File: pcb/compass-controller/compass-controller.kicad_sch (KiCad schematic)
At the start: 75 parts, among them J5 ENCODER BUTTON, J6 LEFT BUTTON, J7 X LIM, J8 X LIM, J9 LEFT BUTTON, SW1 TS1187

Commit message: build platform
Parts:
- added C?: 100n, symbol Device:C_Small
- added J10: PMW_0, symbol Connector_Generic:Conn_01x08
- added J11: PMW_1, symbol Connector_Generic:Conn_01x08
- added J12: PMW_2, symbol Connector_Generic:Conn_01x08
- added J13: PMW_3, symbol Connector_Generic:Conn_01x08
- added J?: TC2030, Connector:Tag-Connect_TC2030-IDC-FP_2x03_P1.27mm_Vertical, symbol Connector:Conn_ARM_SWD_TagConnect_TC2030
- added R57: 220R, symbol Device:R_Small_US
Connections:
- net +3V3: now also J10.1 (Pin_1), J11.1 (Pin_1), J12.1 (Pin_1), J13.1 (Pin_1), J?.1 (VCC)
- net GND: now also J10.3 (Pin_3), J10.5 (Pin_5), J10.7 (Pin_7), J11.3 (Pin_3), J11.5 (Pin_5), J11.7 (Pin_7), J12.3 (Pin_3), J12.5 (Pin_5), J12.7 (Pin_7), J13.3 (Pin_3), J13.5 (Pin_5), J13.7 (Pin_7), J?.5 (GND); no longer J?.A1 (GND), J?.A12 (GND), J?.B1 (GND), J?.B12 (GND)
- net PMW_MISO: now also J10.6 (Pin_6), J11.6 (Pin_6), J12.6 (Pin_6), J13.6 (Pin_6)
- net PMW_MOSI: now also J10.4 (Pin_4), J11.4 (Pin_4), J12.4 (Pin_4), J13.4 (Pin_4)
- net PMW_SCK: now also J10.2 (Pin_2), J11.2 (Pin_2), J12.2 (Pin_2), J13.2 (Pin_2)
- net SWCLK: now also J?.4 (SWCLK)
- net SWDIO: now also J?.2 (SWDIO)
- net ~{nRST}: now also J?.3 (~{RESET})
- net Earth: now reaches J?.S1 (SHIELD)
- net Earth: now also C?.1, R57.1
- new net: C?.2, J?.A1 (GND), J?.A12 (GND), J?.B1 (GND), J?.B12 (GND), R57.2
- new net PMW_CS0: J10.8 (Pin_8)
- new net PMW_CS1: J11.8 (Pin_8)
- new net PMW_CS2: J12.8 (Pin_8)
- new net PMW_CS3: J13.8 (Pin_8)
- no-connect marks 5 -> 6
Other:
- moved on the sheet: J?, R31

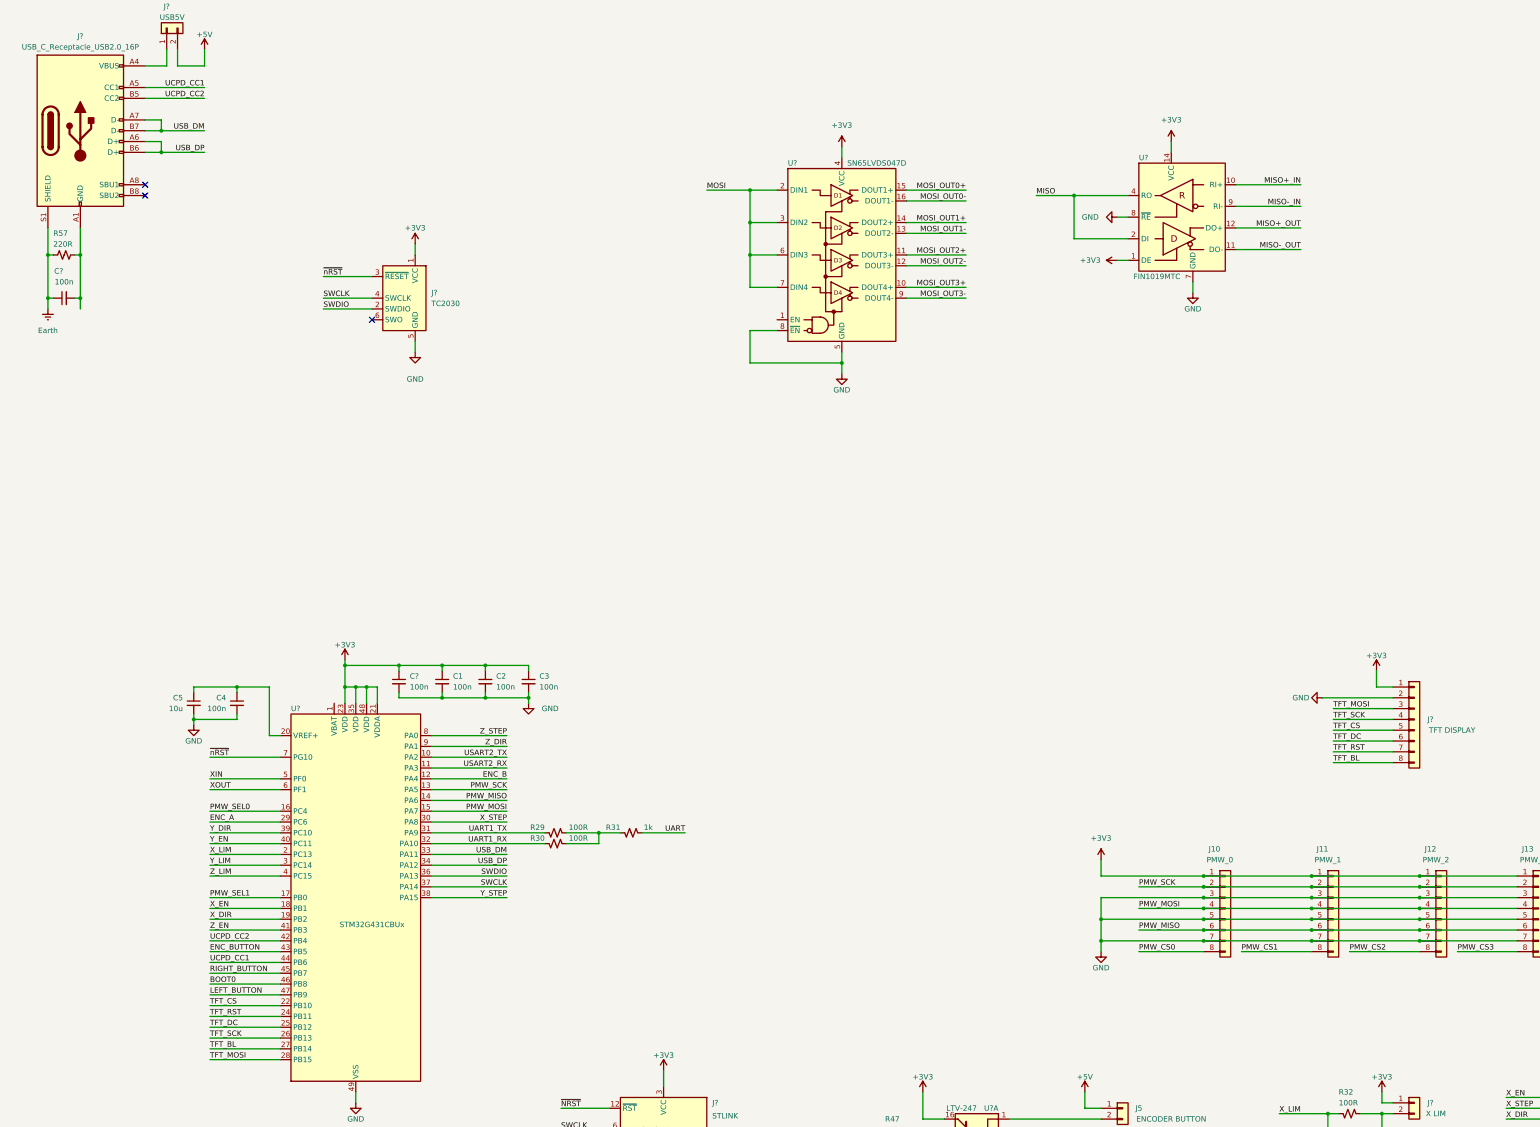
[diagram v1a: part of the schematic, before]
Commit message: update pinout to support SD card
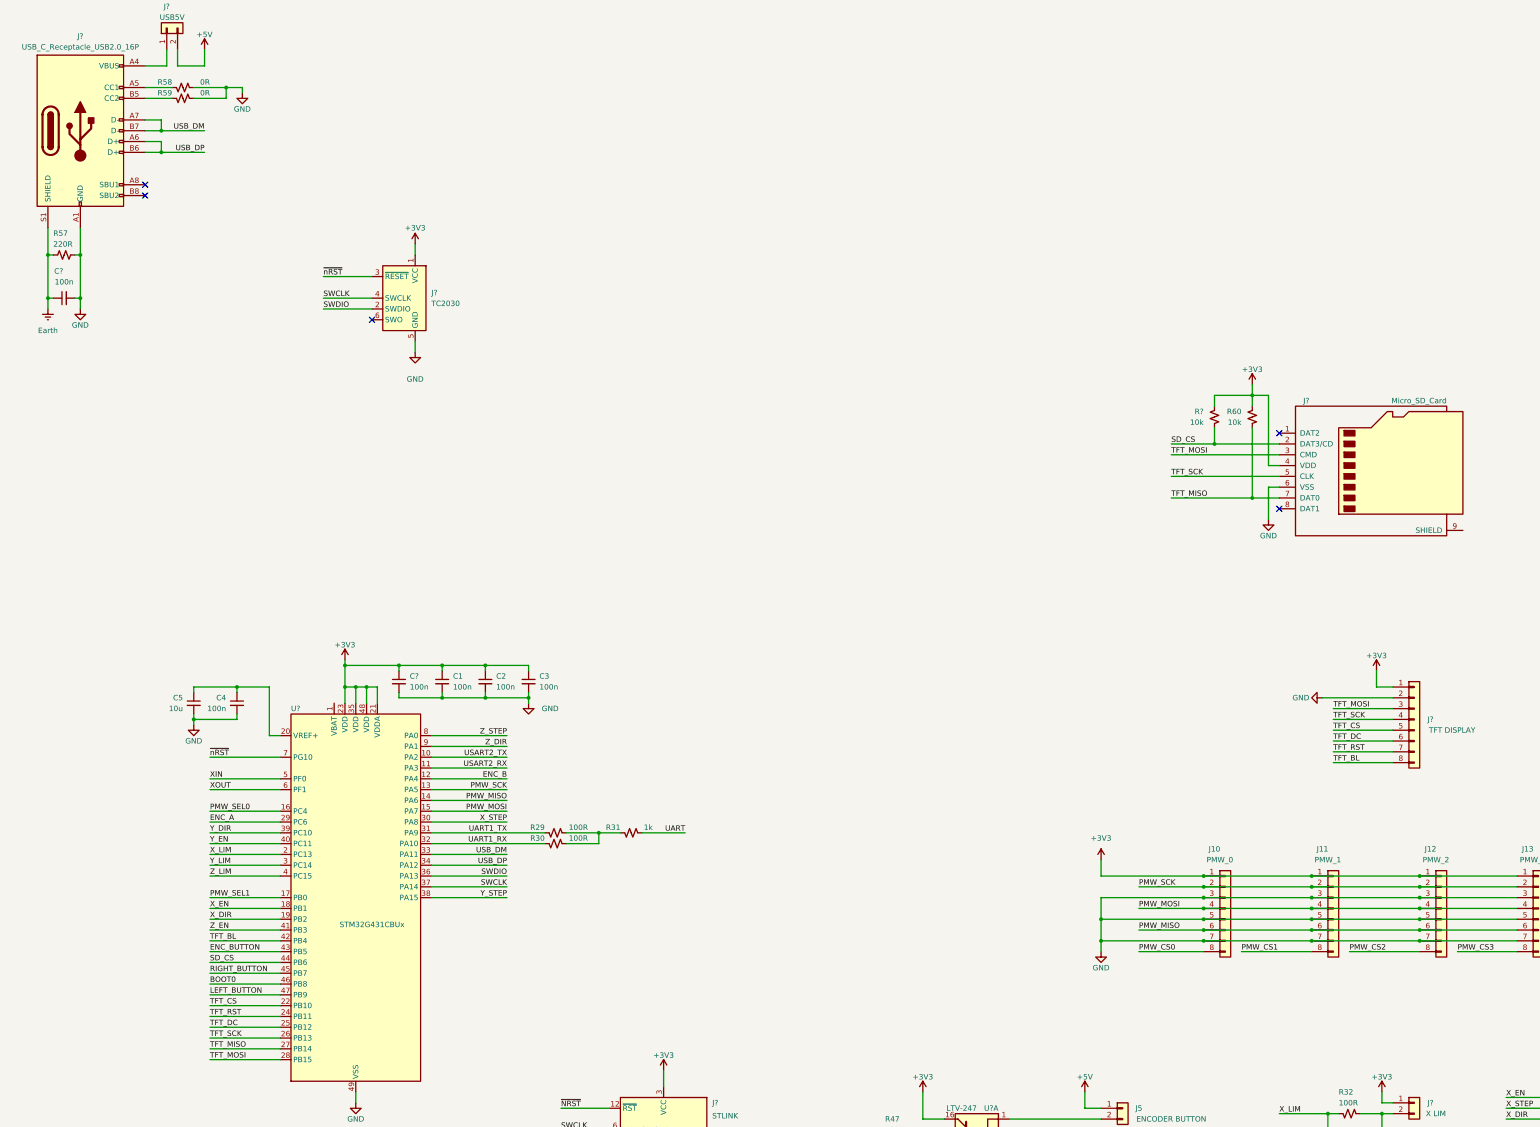
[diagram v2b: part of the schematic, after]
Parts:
- removed U?: FIN1019MTC, Package_SO:TSSOP-14_4.4x5mm_P0.65mm, symbol Interface:FIN1019MTC
- removed U?: SN65LVDS047D, Package_SO:SOIC-16_3.9x9.9mm_P1.27mm, symbol Interface:SN65LVDS047D
- added J?: Micro_SD_Card, symbol Connector:Micro_SD_Card
- added R58, R59: 0R, symbol Device:R_Small_US
- added R60, R?: 10k, symbol Device:R_Small_US
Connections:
- net +3V3: now also J?.4 (VDD), R60.1, R?.1
- net GND: now also C?.2, J?.A1 (GND), J?.A12 (GND), J?.B1 (GND), J?.B12 (GND), R57.2, J?.6 (VSS), R58.2, R59.2
- net TFT_BL: now also U?.42 (PB4); no longer U?.27 (PB14)
- net TFT_MOSI: now also J?.3 (CMD)
- net TFT_SCK: now also J?.5 (CLK)
- net UCPD_CC1: no longer names the net of J?.A5 (CC1)
- net UCPD_CC1: now also R58.1; no longer U?.44 (PB6)
- net UCPD_CC2: no longer names the net of J?.B5 (CC2)
- net UCPD_CC2: now also R59.1; no longer U?.42 (PB4)
- new net SD_CS: J?.2 (DAT3/CD), R?.2, U?.44 (PB6)
- new net TFT_MISO: J?.7 (DAT0), R60.2, U?.27 (PB14)
- no-connect marks 6 -> 8

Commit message: work on schematic
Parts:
- added C301, C305, C306: 10u, Capacitor_SMD:C_1206_3216Metric, symbol Device:C_Small
- added C302: 1u, Capacitor_SMD:C_0603_1608Metric, symbol Device:C_Small
- added C303: 10n, Capacitor_SMD:C_0402_1005Metric, symbol Device:C_Small
- added C304: 100u, Capacitor_SMD:CP_Elec_5x5.4, symbol Device:C_Polarized_Small_US
- added C307: 100n, Capacitor_SMD:C_1206_3216Metric, symbol Device:C_Small
- added D1, D10, D11, D12, D2, D3, D4, D5, D6, D7, D8, D9, D? (x2): WHT, symbol Device:LED
- added D301, D302, D303: SS14, Diode_SMD:D_SMA, symbol Device:D_Schottky
- added J14: Barrel_Jack, symbol Connector:Barrel_Jack
- added L301: 15u, easyeda2kicad:IND-SMD_L8.0-W8.0, symbol Device:L
- added R303: 5k1, Resistor_SMD:R_0603_1608Metric, symbol Device:R_Small_US
- added R304: 100k, Resistor_SMD:R_0603_1608Metric, symbol Device:R_Small_US
- added R305: 10k, Resistor_SMD:R_0603_1608Metric, symbol Device:R_Small_US
- added R306: 3k24, Resistor_SMD:R_0603_1608Metric, symbol Device:R_Small_US
- added R307, R308, R309: 0R, symbol Device:R_Small_US
- added R61: 5k1, symbol Device:R_Small_US
- added R62, R67, R68, R69, R70, R?: 2k2, symbol Device:R_Small_US
- added R63, R64, R65, R66: 10k, symbol Device:R_Small_US
- added R?: 22k, symbol Device:R_Small_US
- added U3, U?: TXU0304PWR, easyeda2kicad:TSSOP-14_L5.0-W4.4-P0.65-LS6.4-BL, symbol easyeda2kicad:TXU0304PWR
- added U301: TPS5430DDA, Package_SO:TI_SO-PowerPAD-8_ThermalVias, symbol Regulator_Switching:TPS5430DDA
- added U?: TPSPX3819M5-L-3-3, easyeda2kicad:SOT-23-5_L3.0-W1.6-P0.95-LS2.8-BR, symbol easyeda2kicad:TPSPX3819M5-L-3-3
- added U?: 74LS138PWR, symbol 74xx:74LS138
- J10, J11, J12, J13: symbol Connector_Generic:Conn_01x08 -> Connector_Generic_Shielded:Conn_01x08_Shielded
- R37, R40, R42, R44, R57: value 220R -> 330R
- R38, R45, R46: value 10k -> 2k2
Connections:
- net +3V3: now also C306.1, C307.1, D2.2 (A), D3.2 (A), D4.2 (A), D5.2 (A), D6.2 (A), D?.2 (A), R308.2, R63.1, R64.1, R65.1, R66.1, U?.16 (VCC)
- net +5V: now also C305.1, D1.2 (A), R307.2, U?.1 (VIN), U?.3 (EN)
- net Earth: now also J10.SH (Shield), J11.SH (Shield), J12.SH (Shield), J13.SH (Shield)
- net GND: now also C301.2, C302.2, C304.2, C305.2, C306.2, C307.2, D301.2 (A), D302.2 (A), J14.2, R303.2, R306.2, R61.2, R62.2, R?.2, U301.6 (GND), U301.9 (GNDPAD), U?.2 (GND), U?.4 (E1), U?.5 (E2), U?.8 (GND)
- net TFT_MISO: no longer J?.7 (DAT0), R60.2
- net TFT_MOSI: no longer J?.3 (CMD), J?.3 (Pin_3)
- net TFT_SCK: no longer J?.4 (Pin_4), J?.5 (CLK)
- net at R43.1, R50.2: now also D10.1 (K); no longer U?.9
- net at R41.1, R49.2: now also D9.1 (K); no longer U?.11
- net at R38.1, R47.2: now also D7.1 (K); no longer U?.15
- net at R45.1, R52.2: now also D12.1 (K); no longer J6.2 (Pin_2)
- net at R46.1, R51.2: now also D11.1 (K); no longer J9.2 (Pin_2)
- net at R39.1, R48.2: now also D8.1 (K); no longer U?.13
- net PMW_CS0 renamed SPI1_CS0
- net SPI1_CS0: now also R?.2, U?.15 (O0)
- net PMW_CS1 renamed SPI1_CS1
- net SPI1_CS1: now also R67.2, U?.14 (O1)
- net PMW_CS2 renamed SPI1_CS2
- net SPI1_CS2: now also R68.2, U?.13 (O2)
- net PMW_CS3 renamed SPI1_CS3
- net SPI1_CS3: now also R69.2, U?.12 (O3)
- net PMW_MISO renamed SPI1_MISO
- net PMW_MOSI renamed SPI1_MOSI
- net SPI1_MOSI: now also J?.3 (Pin_3)
- net PMW_SCK renamed SPI1_SCK
- net SPI1_SCK: now also J?.4 (Pin_4)
- net PMW_SEL0 renamed SPI1_SEL0
- net SPI1_SEL0: now also U?.1 (A0)
- net PMW_SEL1 renamed SPI1_SEL1
- net SPI1_SEL1: now also R64.2, R65.2, U?.2 (A1)
- net TFT_CS renamed SPI1_CS4
- net SPI1_CS4: now also R70.2, U?.11 (O4); no longer U?.22 (PB10)
- new net: D1.1 (K), R61.1
- new net: D2.1 (K), R62.1
- new net: C304.1, D303.2 (A), L301.2, R305.1
- new net: D3.1 (K), R67.1
- new net: D303.1 (K), R307.1
- new net: D?.1 (K), R?.1 (x2)
- new net: D4.1 (K), R68.1
- new net: D9.2 (A), U?.11
- new net: C302.1, R304.2, U301.5 (EN)
- new net: D11.2 (A), J9.2 (Pin_2)
- new net: D6.1 (K), R70.1
- new net: D7.2 (A), U?.15
- new net: D5.1 (K), R69.1
- new net: R308.1, U?.5 (VOUT)
- new net: C303.1, U301.1 (BOOT)
- new net: J14.1, R309.1
- new net: D8.2 (A), U?.13
- new net: D12.2 (A), J6.2 (Pin_2)
- new net: R63.2, U?.6 (E3)
- new net: D10.2 (A), U?.9
- new net +24V: C301.1, D301.1 (K), D?.2 (A), R303.1, R304.1, R309.2, U301.7 (VIN)
- new net FB: R305.2, R306.1, U301.4 (VSENSE)
- new net SPI1_SEL2: R66.2, U?.22 (PB10), U?.3 (A2)
- new net SPI2_MISO: J?.7 (DAT0), R60.2
- new net SPI2_MOSI: J?.3 (CMD)
- new net SPI2_SCK: J?.5 (CLK)
- new net SW: C303.2, D302.1 (K), L301.1, U301.8 (PH)
- no-connect marks 8 -> 12
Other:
- removed sheet POWER SUPPLY
- note added: "can be made exti if helps firmware"
- note added: "output set slightly high to prevent backfeeding +24V0 rail from USB"
- note added: "rated at least 200mW"
- moved on the sheet: C1, C2, C26, C27, C28, C29, C3, C30, C31, C32, C33, C34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

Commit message: finalize schematic, add footprints, start layout
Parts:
- removed C26, C27, C28: 100n, symbol Device:C_Small
- removed C307: 100n, Capacitor_SMD:C_1206_3216Metric, symbol Device:C_Small
- removed D12, D3, D4, D5, D6, D?: WHT, symbol Device:LED
- removed J10: PMW_0, symbol Connector_Generic_Shielded:Conn_01x08_Shielded
- removed J11: PMW_1, symbol Connector_Generic_Shielded:Conn_01x08_Shielded
- removed J12: PMW_2, symbol Connector_Generic_Shielded:Conn_01x08_Shielded
- removed J13: PMW_3, symbol Connector_Generic_Shielded:Conn_01x08_Shielded
- removed J7, J8, J?: X LIM, symbol Connector_Generic:Conn_01x02
- removed R32, R33, R35: 100R, symbol Device:R_Small_US
- removed R34, R36, R63, R64, R65, R66, R?: 10k, symbol Device:R_Small_US
- removed R37, R40, R42: 330R, symbol Device:R_Small_US
- removed R67, R68, R69, R70, R?: 2k2, symbol Device:R_Small_US
- removed U3, U?: TXU0304PWR, easyeda2kicad:TSSOP-14_L5.0-W4.4-P0.65-LS6.4-BL, symbol easyeda2kicad:TXU0304PWR
- removed U?: 74LS138PWR, symbol 74xx:74LS138
- added D103: WHT, Diode_SMD:D_0603_1608Metric, symbol Device:LED
- added H101, H102, H103, H104: M3, MountingHole:MountingHole_3.2mm_M3_DIN965_Pad, symbol Mechanical:MountingHole_Pad
- added R121: 22k, Resistor_SMD:R_0603_1608Metric, symbol Device:R_Small_US
- added R132, R133, R134: 330R, Resistor_SMD:R_0603_1608Metric, symbol Device:R_Small_US
- C101, C105: renamed from C?; footprint (none) -> Capacitor_SMD:C_0603_1608Metric
- C102: renamed from C5; footprint (none) -> Capacitor_SMD:C_1206_3216Metric
- C103: renamed from C4; footprint (none) -> Capacitor_SMD:C_0603_1608Metric
- C104: renamed from C7; footprint (none) -> Capacitor_SMD:C_0402_1005Metric
- C106: renamed from C6; footprint (none) -> Capacitor_SMD:C_0402_1005Metric
- C107: renamed from C1; footprint (none) -> Capacitor_SMD:C_0603_1608Metric
- C108: renamed from C2; footprint (none) -> Capacitor_SMD:C_0603_1608Metric
- C109: renamed from C3; footprint (none) -> Capacitor_SMD:C_0603_1608Metric
- C110: renamed from C32; footprint (none) -> Capacitor_SMD:C_0603_1608Metric
- C111: renamed from C34; footprint (none) -> Capacitor_SMD:C_0603_1608Metric
- C112: renamed from C33; footprint (none) -> Capacitor_SMD:C_0603_1608Metric
- C114: renamed from C302; value 1u -> 10u; footprint Capacitor_SMD:C_0603_1608Metric -> Capacitor_SMD:C_1206_3216Metric
- C115: renamed from C29; footprint (none) -> Capacitor_SMD:C_0603_1608Metric
- C116: renamed from C30; footprint (none) -> Capacitor_SMD:C_0603_1608Metric
- C117: renamed from C31; footprint (none) -> Capacitor_SMD:C_0603_1608Metric
- C119: renamed from C304; value 100u -> 220u
- D101: renamed from D10; footprint (none) -> Diode_SMD:D_0603_1608Metric
- D104: renamed from D11; footprint (none) -> Diode_SMD:D_0603_1608Metric
- D105: renamed from D7; footprint (none) -> Diode_SMD:D_0603_1608Metric
- D106: renamed from D8; footprint (none) -> Diode_SMD:D_0603_1608Metric
- D107: renamed from D9; footprint (none) -> Diode_SMD:D_0603_1608Metric
- D110: renamed from D?; footprint (none) -> Diode_SMD:D_0603_1608Metric
- D111: renamed from D1; footprint (none) -> Diode_SMD:D_0603_1608Metric
- D112: renamed from D2; footprint (none) -> Diode_SMD:D_0603_1608Metric
- J101: renamed from J?; footprint (none) -> Connector_USB:USB_C_Receptacle_GCT_USB4105-xx-A_16P_TopMnt_Horizontal
- J102: renamed from J?; footprint (none) -> Connector_PinHeader_2.54mm:PinHeader_1x02_P2.54mm_Vertical
- J103: renamed from J14; footprint (none) -> Connector_BarrelJack:BarrelJack_GCT_DCJ200-10-A_Horizontal
- J105: renamed from J?; footprint (none) -> Connector_PinHeader_1.27mm:PinHeader_2x07_P1.27mm_Vertical_SMD
- J106: renamed from J6; footprint (none) -> Connector_JST:JST_XH_B2B-XH-A_1x02_P2.50mm_Vertical
- J107: renamed from J9; footprint (none) -> Connector_JST:JST_XH_B2B-XH-A_1x02_P2.50mm_Vertical
- J108: renamed from J?; footprint (none) -> Connector_Card:microSD_HC_Molex_104031-0811
- J109: renamed from J?; footprint (none) -> matei:GC9A01Round1.28
- J110: renamed from J5; footprint (none) -> Connector_JST:JST_XH_B2B-XH-A_1x02_P2.50mm_Vertical
- J111: renamed from J?; footprint (none) -> Connector_JST:JST_XH_B4B-XH-A_1x04_P2.50mm_Vertical
- L101: renamed from L301; footprint easyeda2kicad:IND-SMD_L8.0-W8.0 -> Inductor_SMD:L_Cenker_CKCS8040
- R101: renamed from R57; footprint (none) -> Resistor_SMD:R_0603_1608Metric
- R102: renamed from R58; footprint (none) -> Resistor_SMD:R_0603_1608Metric
- R103: renamed from R59; footprint (none) -> Resistor_SMD:R_0603_1608Metric
- R104: renamed from R54; footprint (none) -> Resistor_SMD:R_0603_1608Metric
- R105: renamed from R53; footprint (none) -> Resistor_SMD:R_0603_1608Metric
- R106: renamed from R29; footprint (none) -> Resistor_SMD:R_0603_1608Metric
- R107: renamed from R30; footprint (none) -> Resistor_SMD:R_0603_1608Metric
- R108: renamed from R31; footprint (none) -> Resistor_SMD:R_0603_1608Metric
- R109: renamed from R50; footprint (none) -> Resistor_SMD:R_0603_1608Metric
- R110: renamed from R55; footprint (none) -> Resistor_SMD:R_0603_1608Metric
- R111: renamed from R56; footprint (none) -> Resistor_SMD:R_0603_1608Metric
- R112: renamed from R43; footprint (none) -> Resistor_SMD:R_0603_1608Metric
- R113: renamed from R309; footprint (none) -> Resistor_SMD:R_0603_1608Metric
- R114: renamed from R52; footprint (none) -> Resistor_SMD:R_0603_1608Metric
- R115: renamed from R51; footprint (none) -> Resistor_SMD:R_0603_1608Metric
- R116: renamed from R45; footprint (none) -> Resistor_SMD:R_0603_1608Metric
- R117: renamed from R46; footprint (none) -> Resistor_SMD:R_0603_1608Metric
- R119: renamed from R44; footprint (none) -> Resistor_SMD:R_0603_1608Metric
- R122, R137: renamed from R?; footprint (none) -> Resistor_SMD:R_0603_1608Metric
- R123: renamed from R60; footprint (none) -> Resistor_SMD:R_0603_1608Metric
- R124: renamed from R47; footprint (none) -> Resistor_SMD:R_0603_1608Metric
- R125: renamed from R48; footprint (none) -> Resistor_SMD:R_0603_1608Metric
- R126: renamed from R49; footprint (none) -> Resistor_SMD:R_0603_1608Metric
- R127: renamed from R38; footprint (none) -> Resistor_SMD:R_0603_1608Metric
- R128: renamed from R39; footprint (none) -> Resistor_SMD:R_0603_1608Metric
- R129: renamed from R41; footprint (none) -> Resistor_SMD:R_0603_1608Metric
- R135: renamed from R307; footprint (none) -> Resistor_SMD:R_0603_1608Metric
- R136: renamed from R308; footprint (none) -> Resistor_SMD:R_0603_1608Metric
- R138: renamed from R23; footprint (none) -> Resistor_SMD:R_0603_1608Metric
- R139: renamed from R24; footprint (none) -> Resistor_SMD:R_0603_1608Metric
- R140: renamed from R25; footprint (none) -> Resistor_SMD:R_0603_1608Metric
- R141: renamed from R26; footprint (none) -> Resistor_SMD:R_0603_1608Metric
- R142: renamed from R27; footprint (none) -> Resistor_SMD:R_0603_1608Metric
- R143: renamed from R28; footprint (none) -> Resistor_SMD:R_0603_1608Metric
- R144: renamed from R61; footprint (none) -> Resistor_SMD:R_0603_1608Metric
- R145: renamed from R62; footprint (none) -> Resistor_SMD:R_0603_1608Metric
- SW101: renamed from SW1; footprint (none) -> easyeda2kicad:SW-SMD_4P-L5.1-W5.1-P3.70-LS6.5-TL_H1.5
- SW102: renamed from SW?; footprint (none) -> easyeda2kicad:SW-SMD_4P-L5.1-W5.1-P3.70-LS6.5-TL_H1.5
- TP101: renamed from TP?; footprint (none) -> TestPoint:TestPoint_Pad_D1.5mm
- TP102: renamed from TP1; footprint (none) -> TestPoint:TestPoint_Pad_D1.5mm
- Y101: renamed from Y?; footprint (none) -> Crystal:Crystal_SMD_SeikoEpson_TSX3225-4Pin_3.2x2.5mm
- gave numbers to parts that had none: 4
- renumbered C301 to C113, C303 to C118, C305 to C120, C306 to C121, D301 to D102, D302 to D108, D303 to D109, R303 to R118, R304 to R120, R305 to R130, R306 to R131, U301 to U103
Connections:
- net SPI1_SEL0 is gone; now on net SPI1_CS0: U101.16 (PC4)
- net SPI1_SEL1 is gone; now on net SPI1_CS1: U101.17 (PB0)
- net SPI1_SEL2 is gone; now on net SPI1_CS2: U101.22 (PB10)
- net SPI2_MISO is gone; now on net SPI1_MISO: J108.7 (DAT0), R123.2
- net SPI2_MOSI is gone; now on net SPI1_MOSI: J108.3 (CMD)
- net SPI2_SCK is gone; now on net SPI1_SCK: J108.5 (CLK)
- net TFT_MISO is gone; now on net SPI1_CS4: U101.27 (PB14)
- net TFT_SCK is gone; now on net SPI1_CS3: U101.26 (PB13)
- net +3V3: now also D101.2 (A), D104.2 (A), D105.2 (A), D106.2 (A), D107.2 (A), D103.2 (A); no longer J106.1 (Pin_1), J107.1 (Pin_1), U102.10, U102.12, U102.14, U102.16
- net Earth: now also J108.9 (SHIELD)
- net GND: now also U102.2, U102.4, U102.6, H101.1, H102.1, H103.1, H104.1, R121.2
- net SD_CS: no longer J108.2 (DAT3/CD), R122.2
- net at J110.2 (Pin_2): now also R132.2; no longer U102.1
- net at R109.2, R112.1: now also U102.9; no longer D101.1 (K)
- net at R126.2, R129.1: now also U102.11; no longer D107.1 (K)
- net at U102.5: now also R134.1; no longer J111.3 (Pin_3)
- net at U102.3: now also R133.1; no longer J111.2 (Pin_2)
- net at R124.2, R127.1: now also U102.15; no longer D105.1 (K)
- net at C114.1, R120.2, U103.5 (EN): now also R121.1
- net at R114.2, R116.1: now also J106.2 (Pin_2)
- net at J107.2 (Pin_2): now also R115.2, R117.1; no longer D104.2 (A)
- net at R125.2, R128.1: now also U102.13; no longer D106.1 (K)
- net TFT_MOSI renamed SPI1_CS5
- net SPI1_CS5: now also J108.2 (DAT3/CD), R122.2
- new net: J111.3 (Pin_3), R134.2
- new net: D103.1 (K), J106.1 (Pin_1)
- new net: J111.2 (Pin_2), R133.2
- new net: D107.1 (K), U102.12
- new net: D104.1 (K), J107.1 (Pin_1)
- new net: R132.1, U102.1
- new net: D105.1 (K), U102.16
- new net: D106.1 (K), U102.14
- new net: D101.1 (K), U102.10
- no-connect marks 12 -> 9
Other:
- added sheet PMW3360_0 (pmw3360.kicad_sch)
- added sheet PMW3360_1 (pmw3360.kicad_sch)
- added sheet PMW3360_2 (pmw3360.kicad_sch)
- added sheet PMW3360_4 (pmw3360.kicad_sch)
- moved on the sheet: C101, C102, C103, C104, C105, C106, C107, C108, C109, C110, C111, C112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

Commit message: work on layout
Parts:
- removed R113: 0R, Resistor_SMD:R_0603_1608Metric, symbol Device:R_Small_US
- removed R118: 5k1, Resistor_SMD:R_0603_1608Metric, symbol Device:R_Small_US
- J107: value LEFT BUTTON -> RIGHT BUTTON
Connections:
- net +24V: now also J103.1
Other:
- note removed: "rated at least 200mW"
- moved on the sheet: C113, D102
